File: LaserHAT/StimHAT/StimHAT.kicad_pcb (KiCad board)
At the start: 4 copper layers, 65 x 57 mm, 112 parts, among them J1 GPIO, J10 OLED 0.91 (GND VCC SCL SDA), J101 ELECTRODE E1/E2, J102 B4B-PH-K-S(LF)(SN), J103 5V TO DC-DC POD, J5 GT-USB-7010ASV, J6 BNC TRIGGER IN, J7 BNC STIM OUT, Q3 AP30P30Q, Q4 DMMT5401, Q5 AP30P30Q, SW10 MSK12C02, SW6 TS-1088-AR02016, SW7 SKRHADE010, SW9 TS-1088-AR02016, U1 M24C32-WDW6TP, U101 ISO7741FDBQR, U104 TLV76050DBZR, U105 DAC60501ZDGSR, U106 OPA2192IDGKR, U107 CD74HC4053PWR, U108 DG418DY-T1-E3, U109 ISO1640BDR, U110 TLV1702AIDGKR, U4 MCP1700T-3302E/MB, U5 AP2171W, U6 CH340N, U7 MSPM0G1507SRHBR, U8 74LVC2G17GW

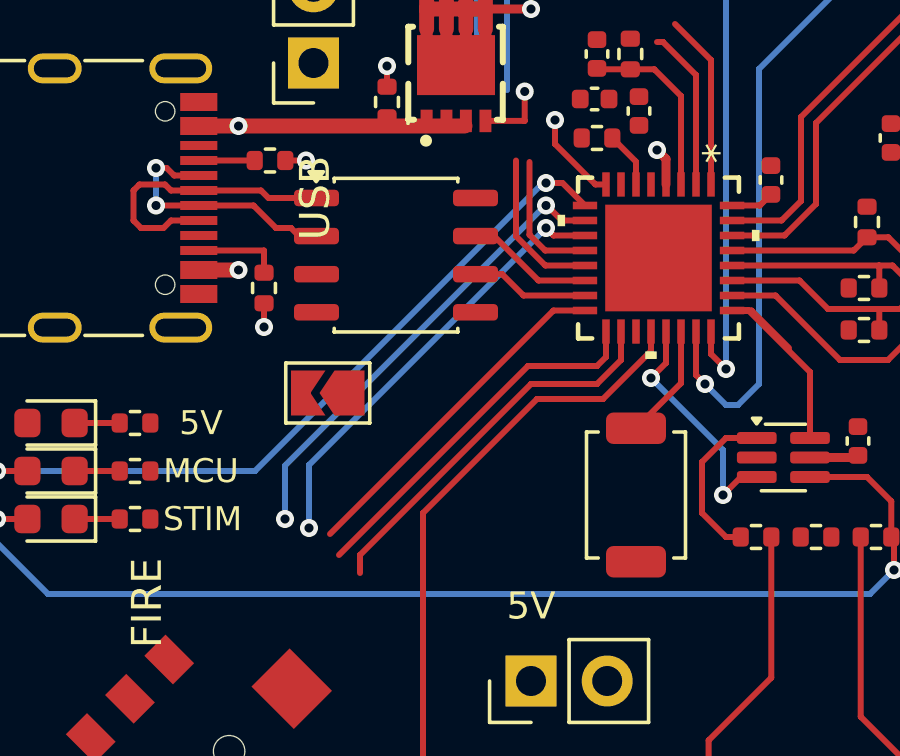
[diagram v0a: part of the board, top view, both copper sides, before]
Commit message: StimHAT: header pins and joystick fan-out re-mapped for routing
Pi header (user's request): PI_TRIGGER -> GPIO18 (pin 12), MCU_PWR_EN -> GPIO10 (pin 19),
NRST -> GPIO9 (pin 21), all in the west half above U7; pins 11 / 13 / 15 are bonnet buttons and
24 / 26 pull up at boot, so NRST takes 21.  Pi side: LASERHAT_NRST_PIN=9 LASERHAT_POWER_PIN=10
LASERHAT_TRIGGER_PIN=18, brokerd --gpio-pin 18.

U7: LED_MCU 9 -> 10 (PA6, frees the PI_RXD / PI_TXD via spot), buttons on 11 / 16 / 17 / 18 / 19
(PA7 / 12 / 13 / 14 / 15) as a 45-degree fan to SW7 in its pad order, FIRE stays on 20.  SW7 at
the user's 135-degree rotation: contact A (pad 1) = down, B (4) = left, C (3) = right, D (6) = up,
nets re-wired to match.  The partly routed BUTTON1/2/3/4/6 copper was ripped (BUTTON5 kept), the
LED's via re-hooked from pin 10.

Schematic regenerated (netcheck OK, ERC 0), nets pushed into the board with the tracks kept
(path / sync checks 0), DRC 0 errors, 49 open connections.  README and placement table updated.

Co-Authored-By: Claude Fable 5.1 <noreply@anthropic.com>
Claude-Session: https://claude.ai/code/session_015kiXLxnPpBaXdXJu2EMvn7
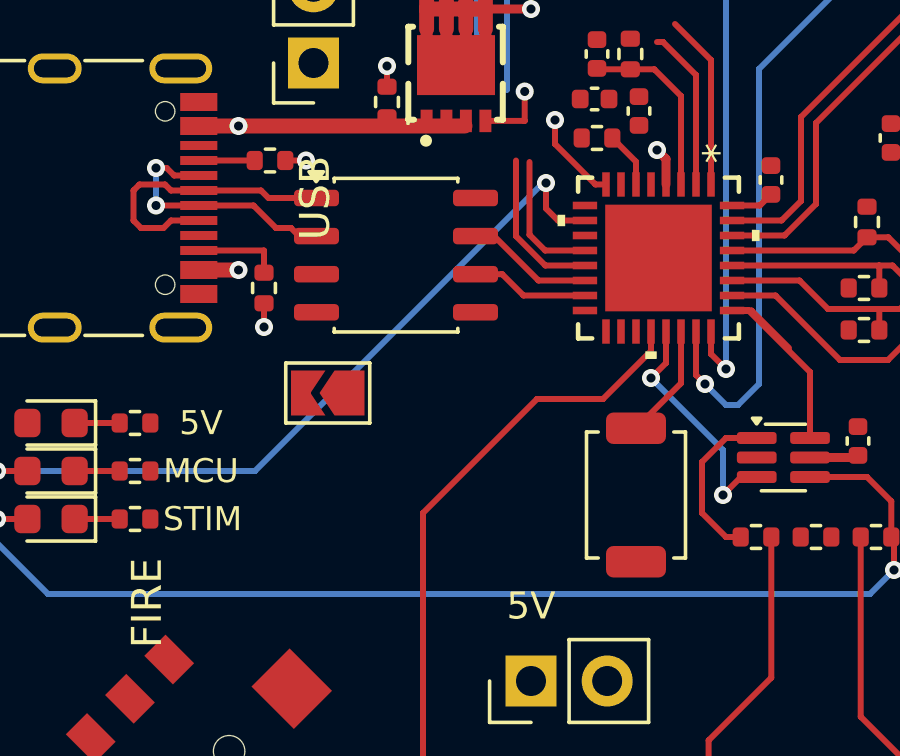
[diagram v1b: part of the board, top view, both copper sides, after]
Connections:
- J1 pad 12: MCU_PWR_EN -> PI_TRIGGER
- J1 pad 19: PI_TRIGGER -> MCU_PWR_EN
- J1 pad 21: unconnected-(J1-GPIO9-Pad21) -> NRST
- J1 pad 36: NRST -> unconnected-(J1-GPIO16-Pad36)
- SW7 pad 1: BUTTON4 -> BUTTON3
- SW7 pad 3: BUTTON1 -> BUTTON6
- SW7 pad 4: BUTTON6 -> BUTTON1
- SW7 pad 6: BUTTON3 -> BUTTON4
- U7 pad 10: BUTTON4 -> LED_MCU
- U7 pad 11: BUTTON6 -> BUTTON1
- U7 pad 16: BUTTON2 -> BUTTON4
- U7 pad 17: BUTTON1 -> BUTTON6
- U7 pad 18: BUTTON3 -> BUTTON2
- U7 pad 19: unconnected-(U7-PA15/DAC-Pad19) -> BUTTON3
- U7 pad 9: LED_MCU -> unconnected-(U7-PA5-Pad9)
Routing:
- net BUTTON4: track 15.6 -> 0.00 mm, vias 2 -> 0
- net BUTTON6: track 14.7 -> 0.00 mm, vias 2 -> 0
- net BUTTON3: track 12.9 -> 0.00 mm
- net BUTTON1: track 12.5 -> 0.00 mm
- net BUTTON2: track 11.6 -> 0.00 mm
- net LED_MCU: track 25.1 -> 25.8 mm
